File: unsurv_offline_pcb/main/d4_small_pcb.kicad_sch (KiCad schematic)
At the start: 52 parts, among them J1 U_FL-R-SMT-1_10_, J2 S2B-PH-SM4-TB_LF__SN_, Q1 UMH3N, U1 TTGO-Micro32-ESP32, U3 CAM-M8C-0-10, U4 AP2112K-3.3, U5 CH340G, U6 RF430CL330H, U7 BMA400-I2C, U8 RFM95W-868S2, U9 PQ2581DLHT

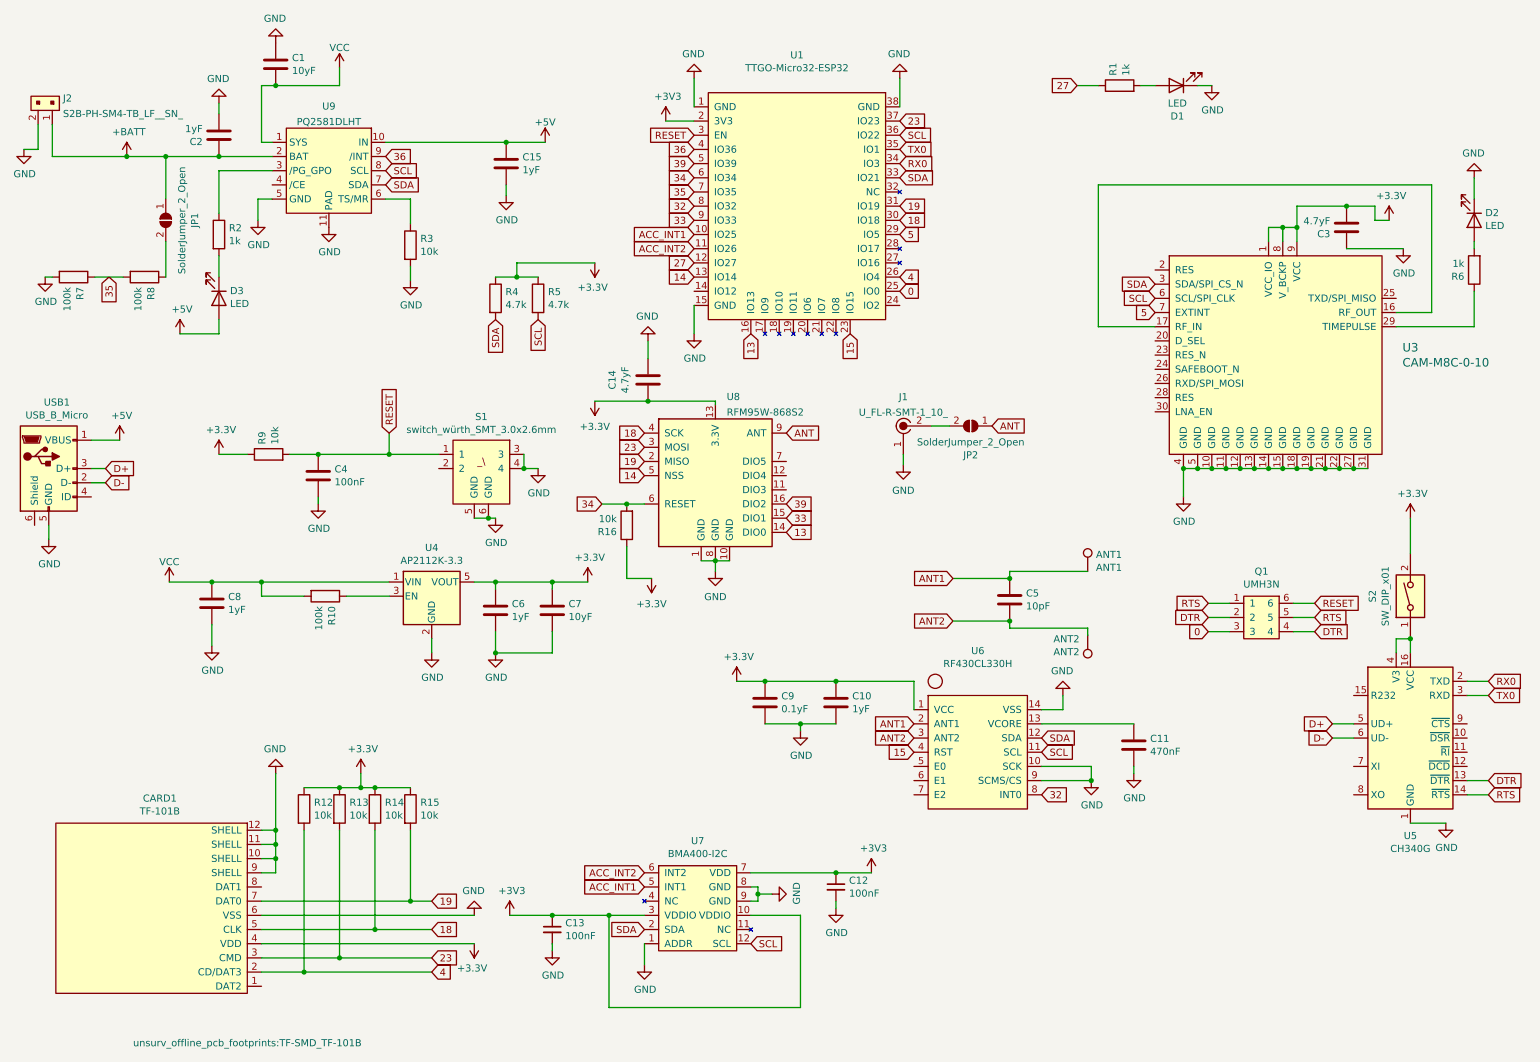
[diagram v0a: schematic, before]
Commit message: moving passives around BQ25181
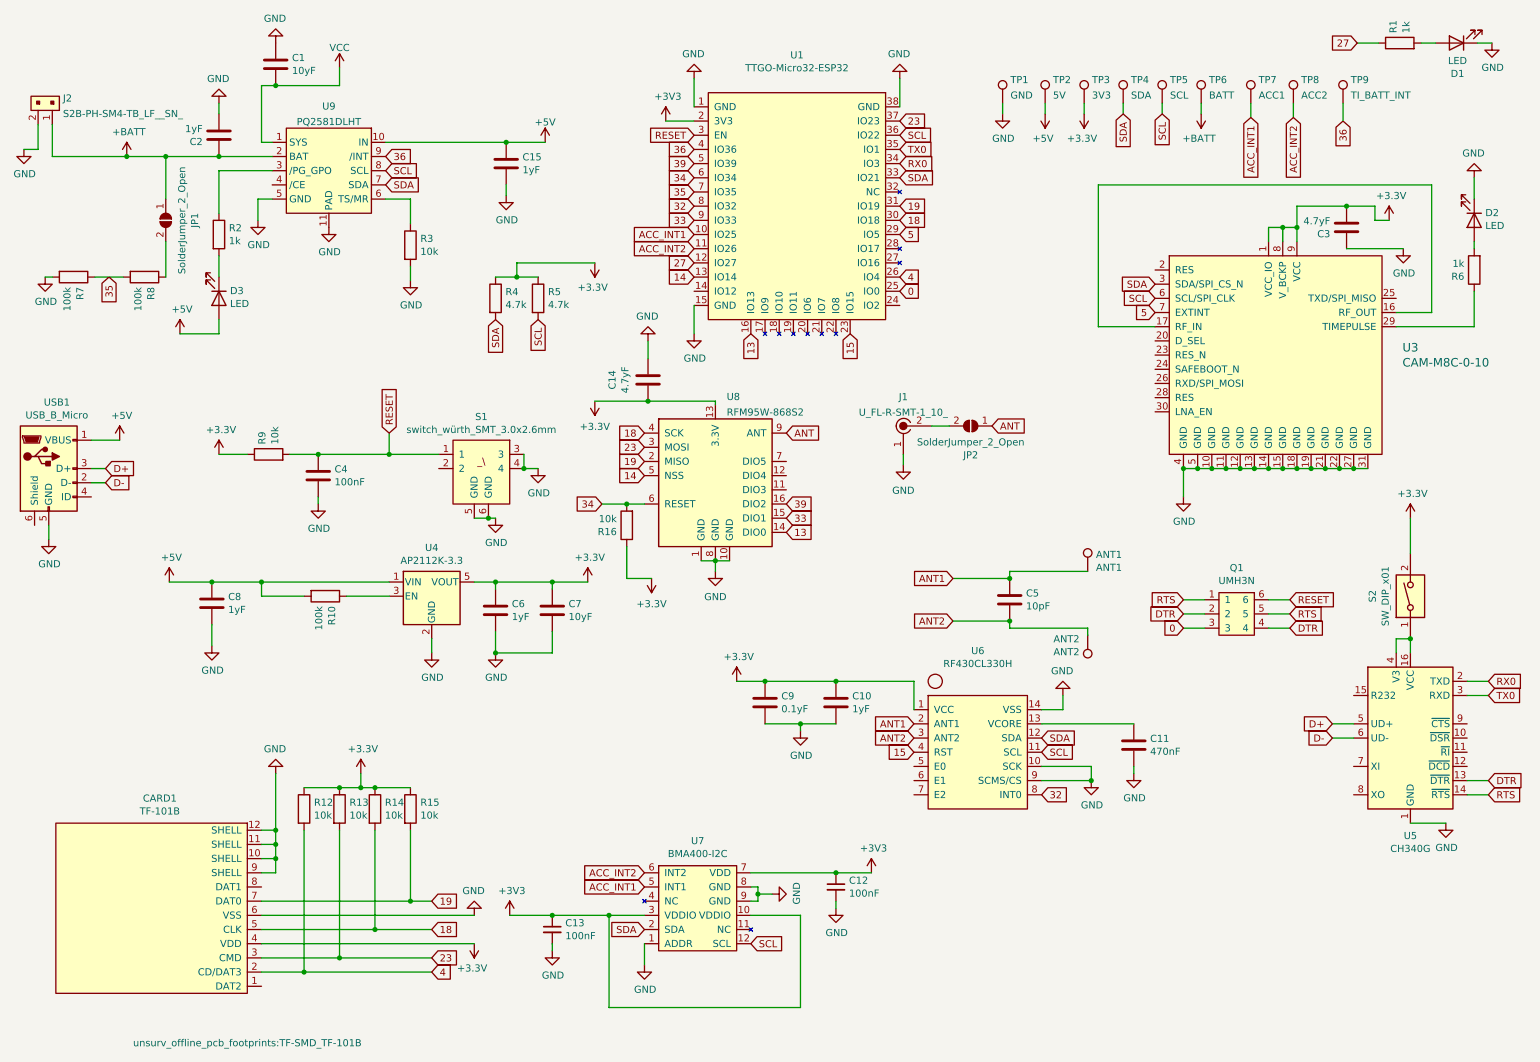
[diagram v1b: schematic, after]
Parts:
- added TP1: GND, TestPoint:TestPoint_Pad_D1.0mm, symbol Connector:TestPoint
- added TP2: 5V, TestPoint:TestPoint_Pad_D1.0mm, symbol Connector:TestPoint
- added TP3: 3V3, TestPoint:TestPoint_Pad_D1.0mm, symbol Connector:TestPoint
- added TP4: SDA, TestPoint:TestPoint_Pad_D1.0mm, symbol Connector:TestPoint
- added TP5: SCL, TestPoint:TestPoint_Pad_D1.0mm, symbol Connector:TestPoint
- added TP6: BATT, TestPoint:TestPoint_Pad_D1.0mm, symbol Connector:TestPoint
- added TP7: ACC1, TestPoint:TestPoint_Pad_D1.0mm, symbol Connector:TestPoint
- added TP8: ACC2, TestPoint:TestPoint_Pad_D1.0mm, symbol Connector:TestPoint
- added TP9: TI_BATT_INT, TestPoint:TestPoint_Pad_D1.0mm, symbol Connector:TestPoint
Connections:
- net +3V3: now also TP3.1
- net +5V: now also C8.2, R10.2, U4.1 (VIN), TP2.1
- net +BATT: now also TP6.1
- net 36: now also TP9.1
- net ACC_INT1: now also TP7.1
- net ACC_INT2: now also TP8.1
- net GND: now also TP1.1
- net SCL: now also TP5.1
- net SDA: now also TP4.1
- net VCC: no longer C8.2, R10.2, U4.1 (VIN)
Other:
- moved on the sheet: D1, Q1, R1

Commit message: update RF430 package to VQFN
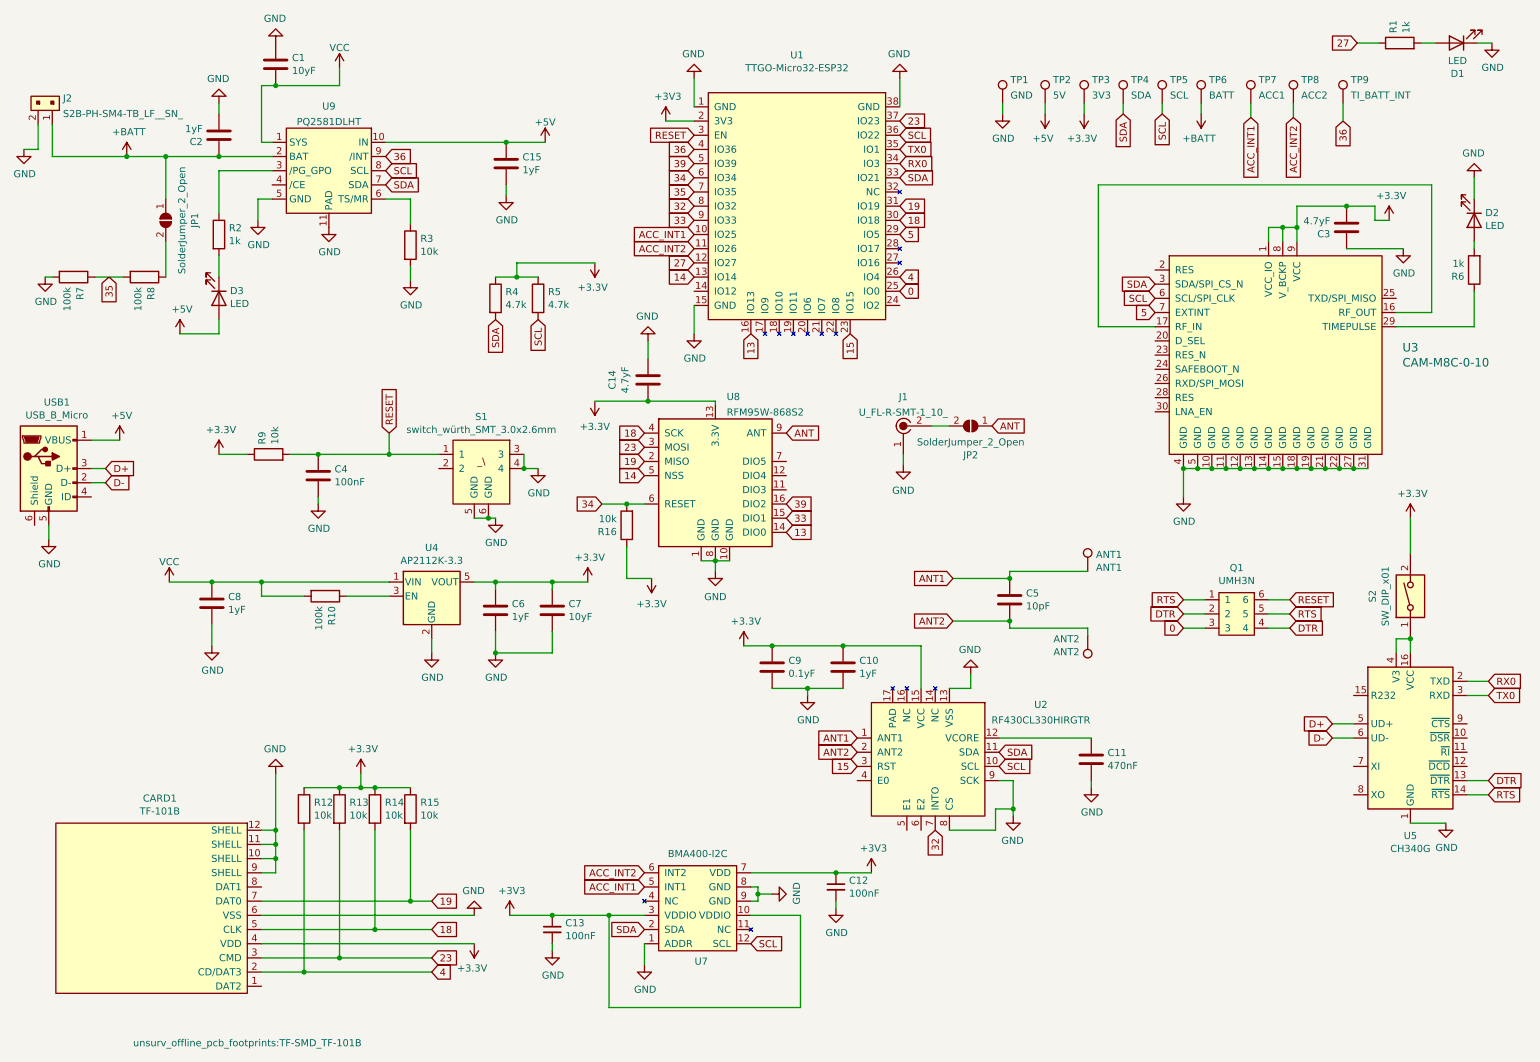
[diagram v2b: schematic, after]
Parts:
- removed U6: RF430CL330H, unsurv_offline_pcb_footprints:RF430CL330H, symbol unsurv_offline_pcb_symbols:RF430CL330H
- added U2: RF430CL330HIRGTR‎, unsurv_offline_pcb_footprints:RF430_3x3mm, symbol unsurv_offline_pcb_symbols:RF430CL330HIRGTR‎
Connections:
- net +3V3: now also U2.15 (VCC)
- net +5V: no longer C8.2, R10.2, U4.1 (VIN)
- net 15: now also U2.3 (RST)
- net 32: now also U2.7 (INTO)
- net ANT1: now also U2.1 (ANT1)
- net ANT2: now also U2.2 (ANT2)
- net GND: now also U2.13 (VSS), U2.8 (CS), U2.9 (SCK)
- net SCL: now also U2.10 (SCL)
- net SDA: now also U2.11 (SDA)
- net VCC: now also C8.2, R10.2, U4.1 (VIN)
- net at C11.1: now also U2.12 (VCORE)
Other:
- moved on the sheet: C10, C11, C9

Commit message: reorganize passives
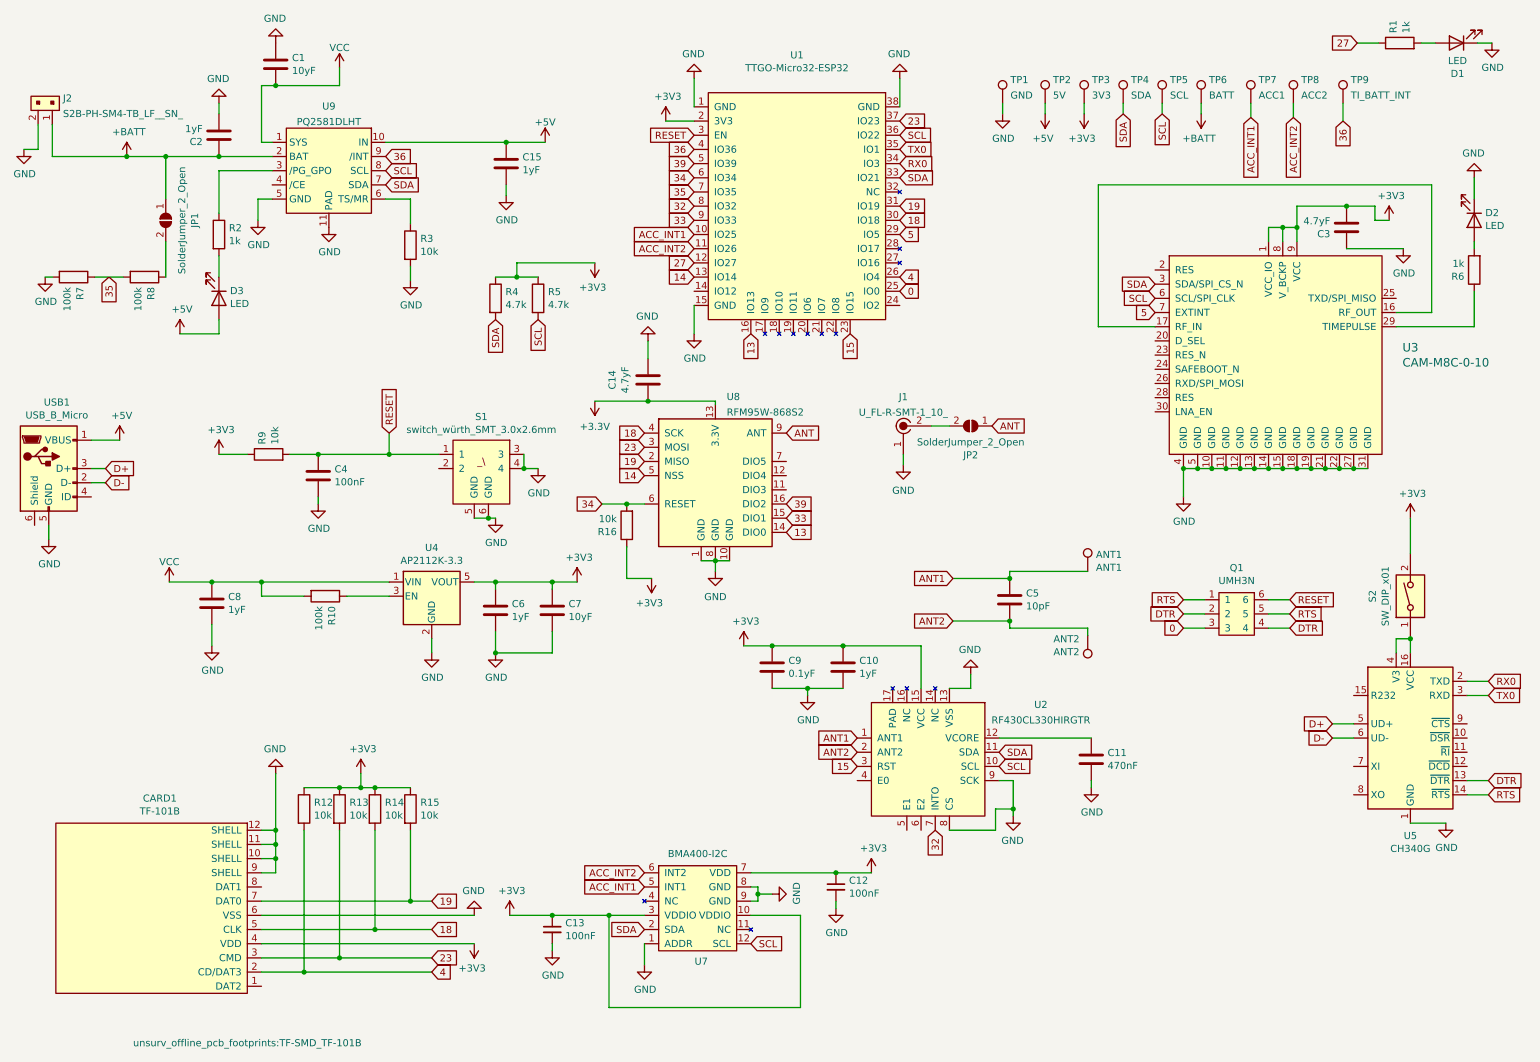
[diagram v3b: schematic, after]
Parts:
- U3: footprint unsurv_offline_pcb_footprints:GPS_Module_CAM-M8C-0 -> digikey-footprints:GPS_Module_CAM-M8C-0
- U9: footprint unsurv_offline_pcb_footprints:BQ2581DLHT -> unsurv:BQ2581DLHT
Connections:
- net +3V3: no longer C14.2, U8.13 (3.3V)
- new net +3.3V: C14.2, U8.13 (3.3V)

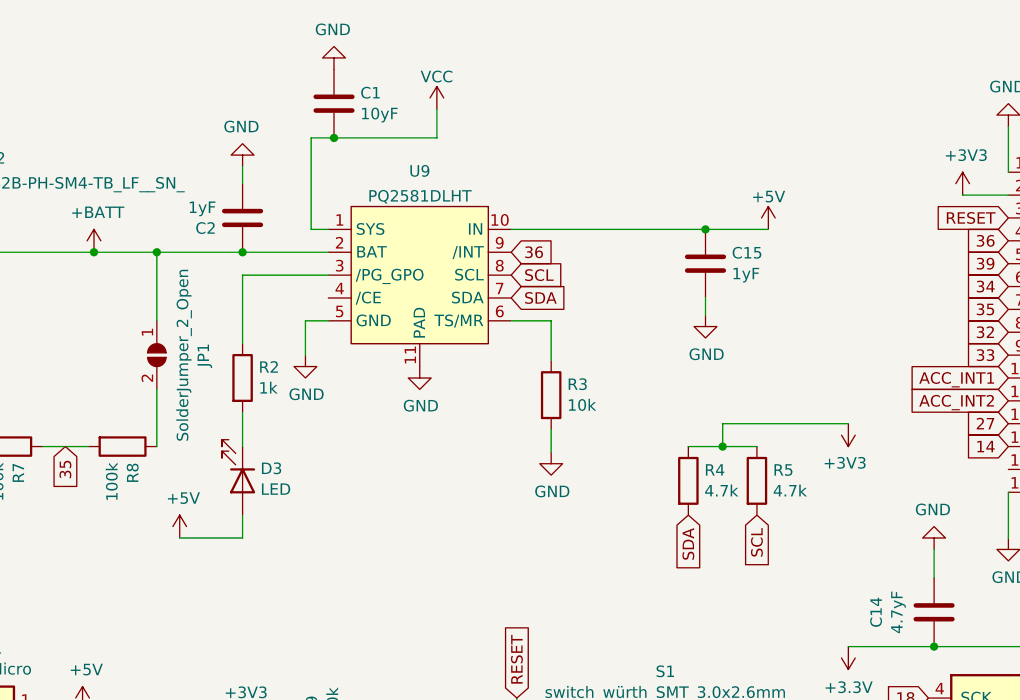
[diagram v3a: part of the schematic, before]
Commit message: BQ25180 redesign
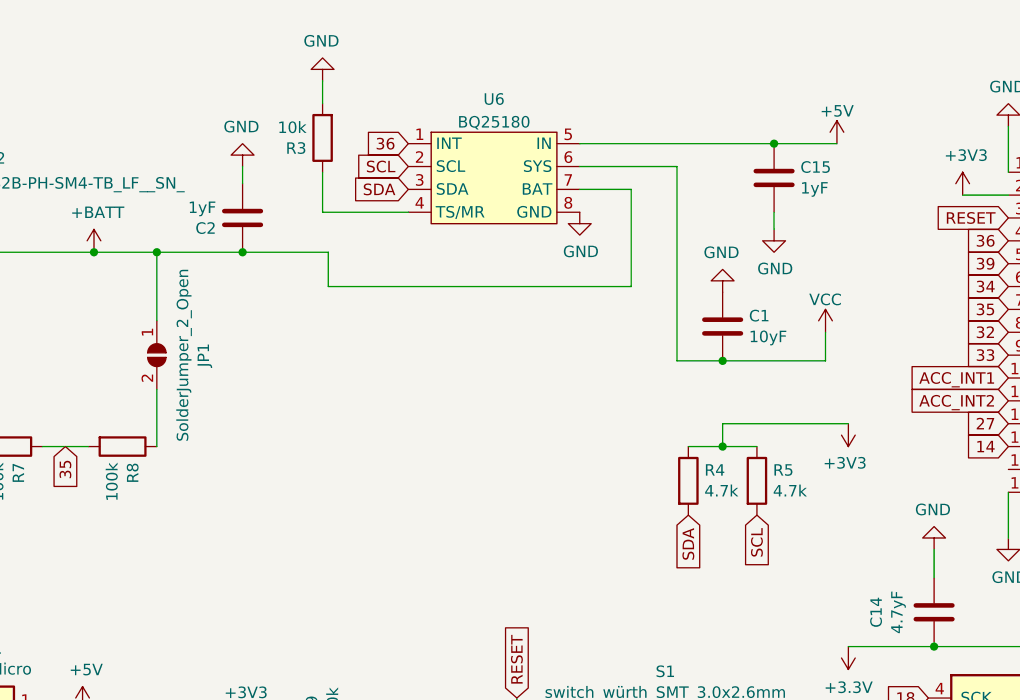
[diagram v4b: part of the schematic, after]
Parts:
- removed D3: LED, digikey-footprints:LED_0603, symbol Device:LED
- removed R2: 1k, Resistor_SMD:R_0603_1608Metric, symbol Device:R
- removed U9: PQ2581DLHT, unsurv:BQ2581DLHT, symbol unsurv_offline_pcb_symbols:PQ2581DLHT
- added U6: BQ25180, unsurv:BQ25180, symbol unsurv_offline_pcb_symbols:BQ25180
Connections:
- net +5V: now also U6.5 (IN)
- net +BATT: now also U6.7 (BAT)
- net 36: now also U6.1 (INT)
- net GND: now also U6.8 (GND)
- net SCL: now also U6.2 (SCL)
- net SDA: now also U6.3 (SDA)
- net VCC: now also U6.6 (SYS)
- net at R3.1: now also U6.4 (TS/MR)
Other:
- moved on the sheet: C1, C15, R3

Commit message: pre-production run
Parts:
- U2: footprint unsurv_offline_pcb_footprints:RF430_3x3mm -> unsurv_offline_pcb_footprints:RF430_3x3mm_regular
- U7: footprint unsurv_offline_pcb_footprints:BMA400 -> unsurv_offline_pcb_footprints:BMA400_regular
